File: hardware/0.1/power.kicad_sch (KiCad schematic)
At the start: 30 parts, among them U1 ECP5U_12_CABGA256, U2 TLV73325PDBV, U3 TLV62568DBV, U5 TLV62568DBV

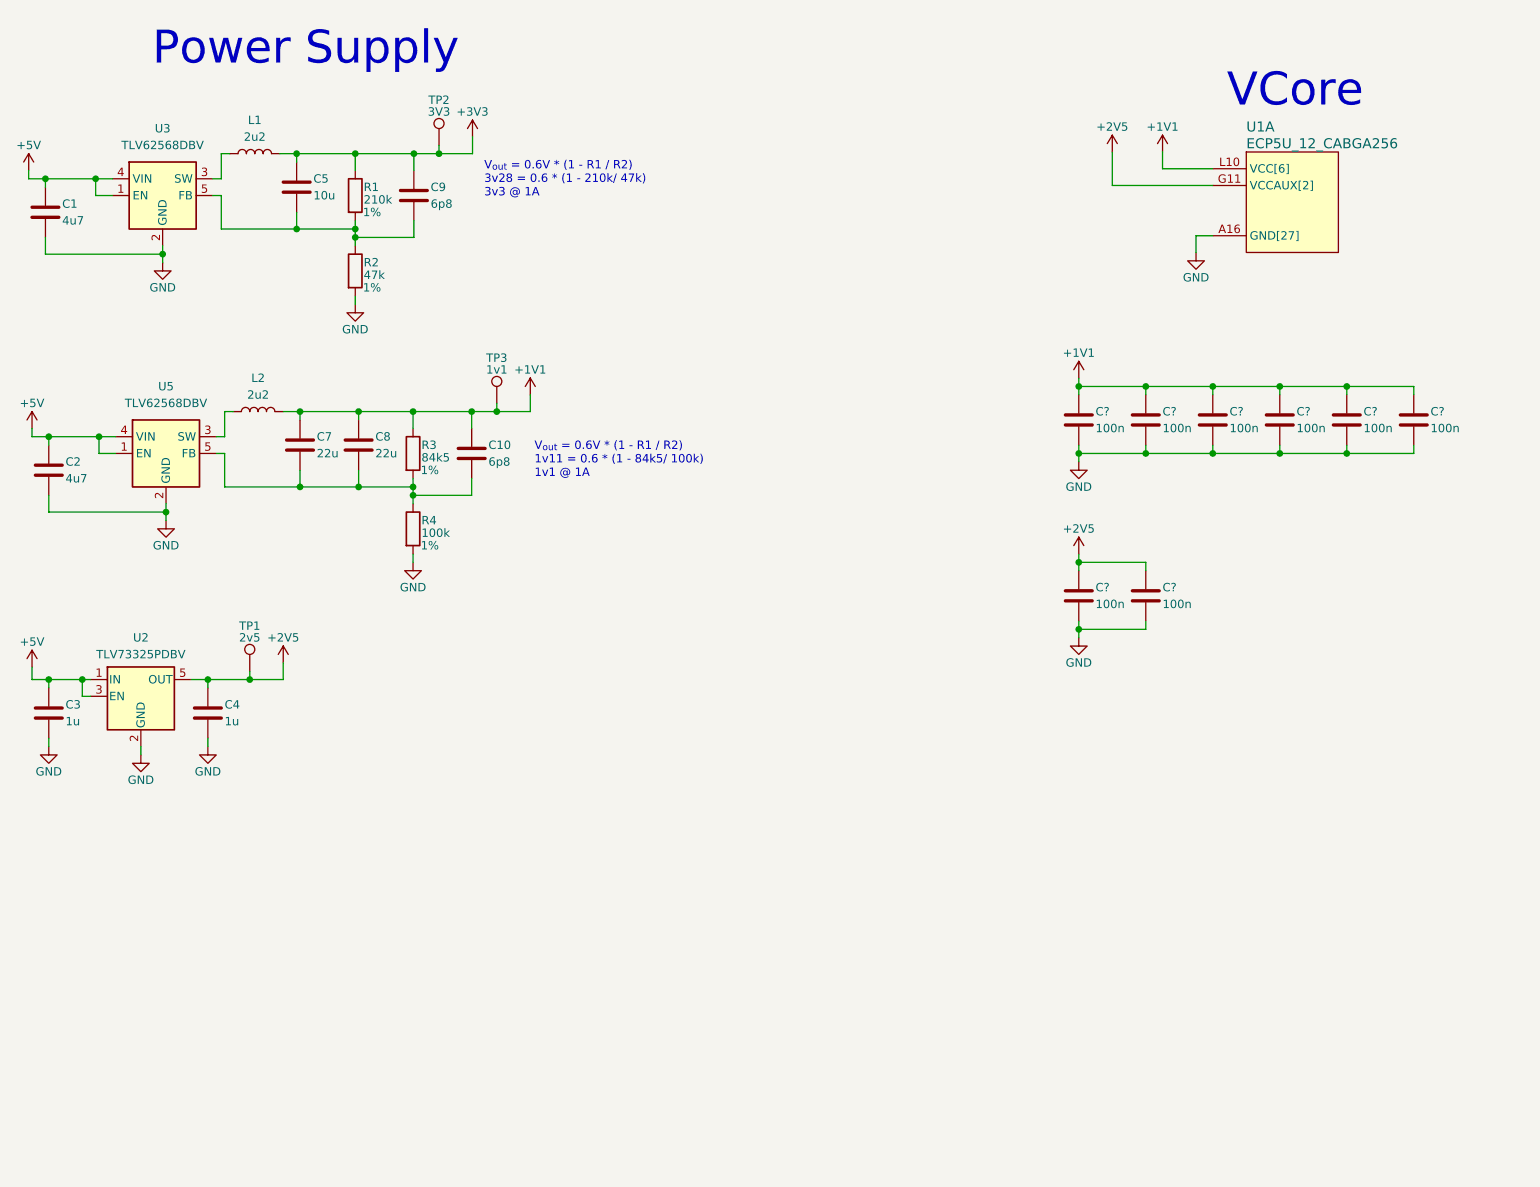
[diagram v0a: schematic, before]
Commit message: all 3d models added
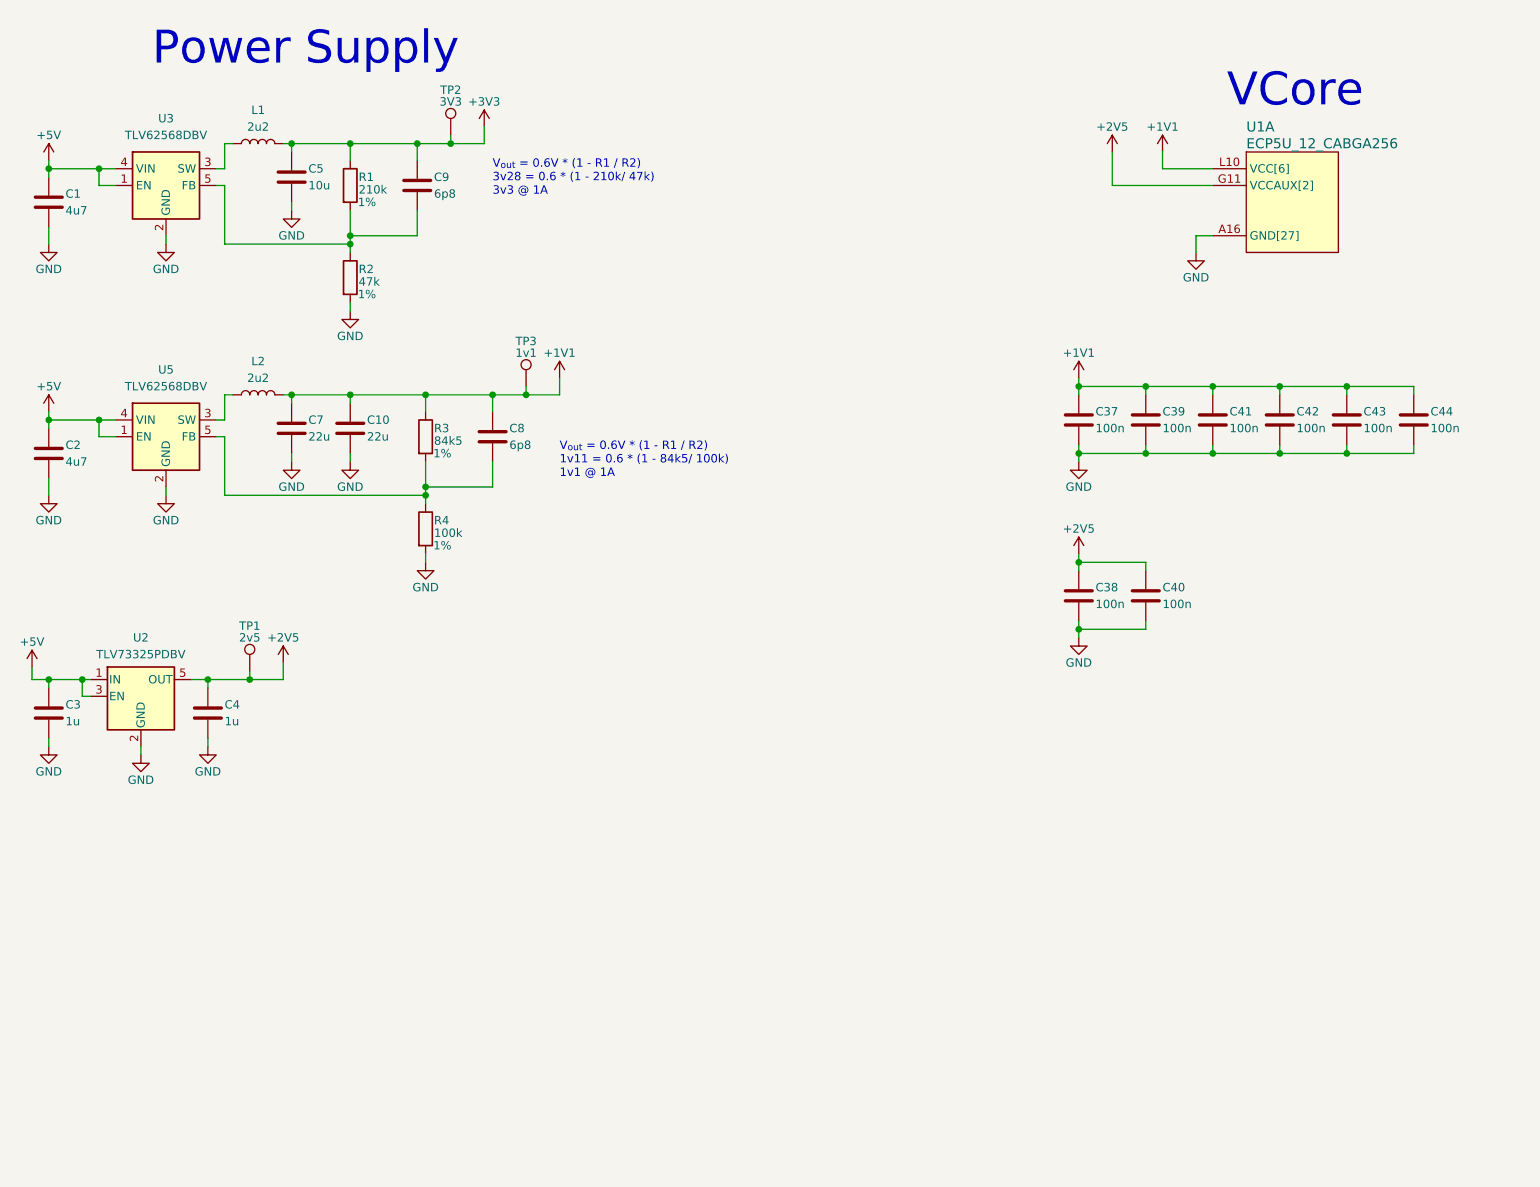
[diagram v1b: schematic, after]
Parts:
- C10: value 6p8 -> 22u
- C8: value 22u -> 6p8; footprint Capacitor_SMD:C_0603_1608Metric -> Capacitor_SMD:C_0402_1005Metric
- C9: footprint Capacitor_SMD:C_0603_1608Metric -> Capacitor_SMD:C_0402_1005Metric
- gave numbers to parts that had none: 8
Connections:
- net GND: now also C10.2, C5.2, C7.2
- net at C8.2, R3.2, R4.1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: no longer C10.2, C7.2
- net at C9.2, R1.2, R2.1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: no longer C5.2
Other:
- moved on the sheet: C1, C5, C9, L1, R1, R2, TP2, U3

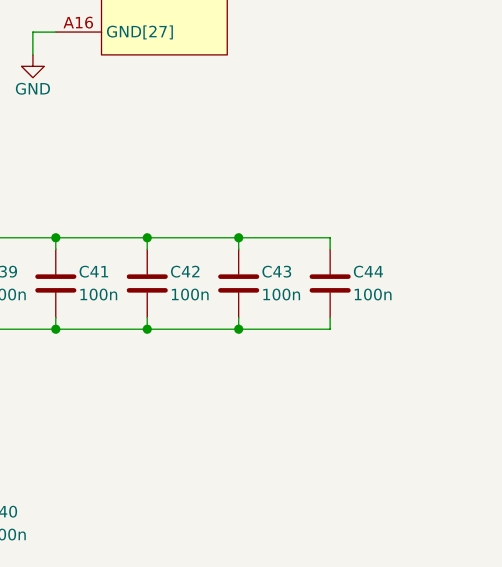
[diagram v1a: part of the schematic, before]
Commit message: decoupling down + outer pins fanned out
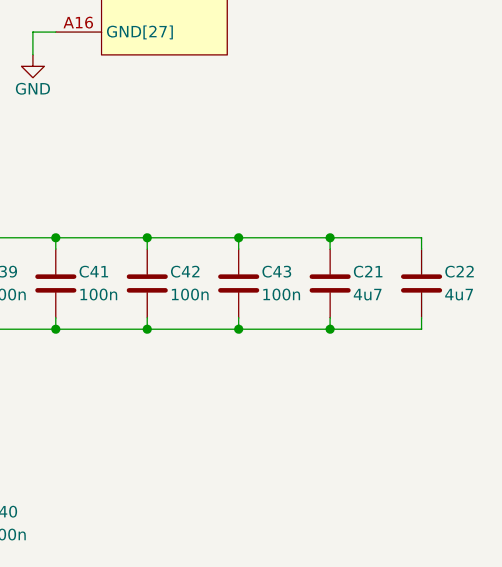
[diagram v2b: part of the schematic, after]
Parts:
- removed C44: 100n, Capacitor_SMD:C_0402_1005Metric, symbol Device:C
- added C21, C22: 4u7, Capacitor_SMD:C_0402_1005Metric, symbol Device:C
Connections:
- net +1V1: now also C21.1, C22.1
- net GND: now also C21.2, C22.2
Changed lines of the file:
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@@
   (junction (at 223.52 76.2) (diameter 1.016) (color 0 0 0 0))
   (junction (at 223.52 86.36) (diameter 1.016) (color 0 0 0 0))
+  (junction (at 233.68 76.2) (diameter 1.016) (color 0 0 0 0))
+  (junction (at 233.68 86.36) (diameter 1.016) (color 0 0 0 0))
   (wire (pts (xy 24.13 118.745) (xy 24.13 120.65))
     (stroke (width 0) (type solid) (color 0 0 0 0))
@@
     (stroke (width 0) (type solid) (color 0 0 0 0))
   )
+  (wire (pts (xy 233.68 76.2) (xy 243.84 76.2))
+    (stroke (width 0) (type solid) (color 0 0 0 0))
+  )
   (wire (pts (xy 233.68 85.09) (xy 233.68 86.36))
+    (stroke (width 0) (type solid) (color 0 0 0 0))
+  )
+  (wire (pts (xy 233.68 86.36) (xy 243.84 86.36))
+    (stroke (width 0) (type solid) (color 0 0 0 0))
+  )
+  (wire (pts (xy 243.84 76.2) (xy 243.84 77.47))
+    (stroke (width 0) (type solid) (color 0 0 0 0))
+  )
+  (wire (pts (xy 243.84 85.09) (xy 243.84 86.36))
     (stroke (width 0) (type solid) (color 0 0 0 0))
   )
@@
   (symbol (lib_id "Device:C") (at 233.68 81.28 0) (unit 1)
     (in_bom yes) (on_board yes)
-    (property "Reference" "C44" (id 0) (at 236.22 80.01 0)
-      (effects (font (size 1.27 1.27)) (justify left))
-    )
-    (property "Value" "100n" (id 1) (at 236.22 82.55 0)
+    (property "Reference" "C21" (id 0) (at 236.22 80.01 0)
+      (effects (font (size 1.27 1.27)) (justify left))
+    )
+    (property "Value" "4u7" (id 1) (at 236.22 82.55 0)
       (effects (font (size 1.27 1.27)) (justify left))
     )
@@
       (effects (font (size 1.27 1.27)) hide)
     )
+  )
+  (symbol (lib_id "Device:C") (at 243.84 81.28 0) (unit 1)
+    (in_bom yes) (on_board yes)
+    (property "Reference" "C22" (id 0) (at 246.38 80.01 0)
+      (effects (font (size 1.27 1.27)) (justify left))
+    )
+    (property "Value" "4u7" (id 1) (at 246.38 82.55 0)
+      (effects (font (size 1.27 1.27)) (justify left))
+    )
+    (property "Footprint" "Capacitor_SMD:C_0402_1005Metric" (id 2) (at 244.8052 85.09 0)
+      (effects (font (size 1.27 1.27)) hide)
+    )
+    (property "Datasheet" "~" (id 3) (at 243.84 81.28 0)
+      (effects (font (size 1.27 1.27)) hide)
+    )
